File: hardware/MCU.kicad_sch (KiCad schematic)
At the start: 38 parts, among them J2 Micro_SD_Card, J3 USB_C_Receptacle, SW2 SW_Push, SW3 SW_Push, U7 ESP32-S3-WROOM-1, U8 WE-TVS-82400102

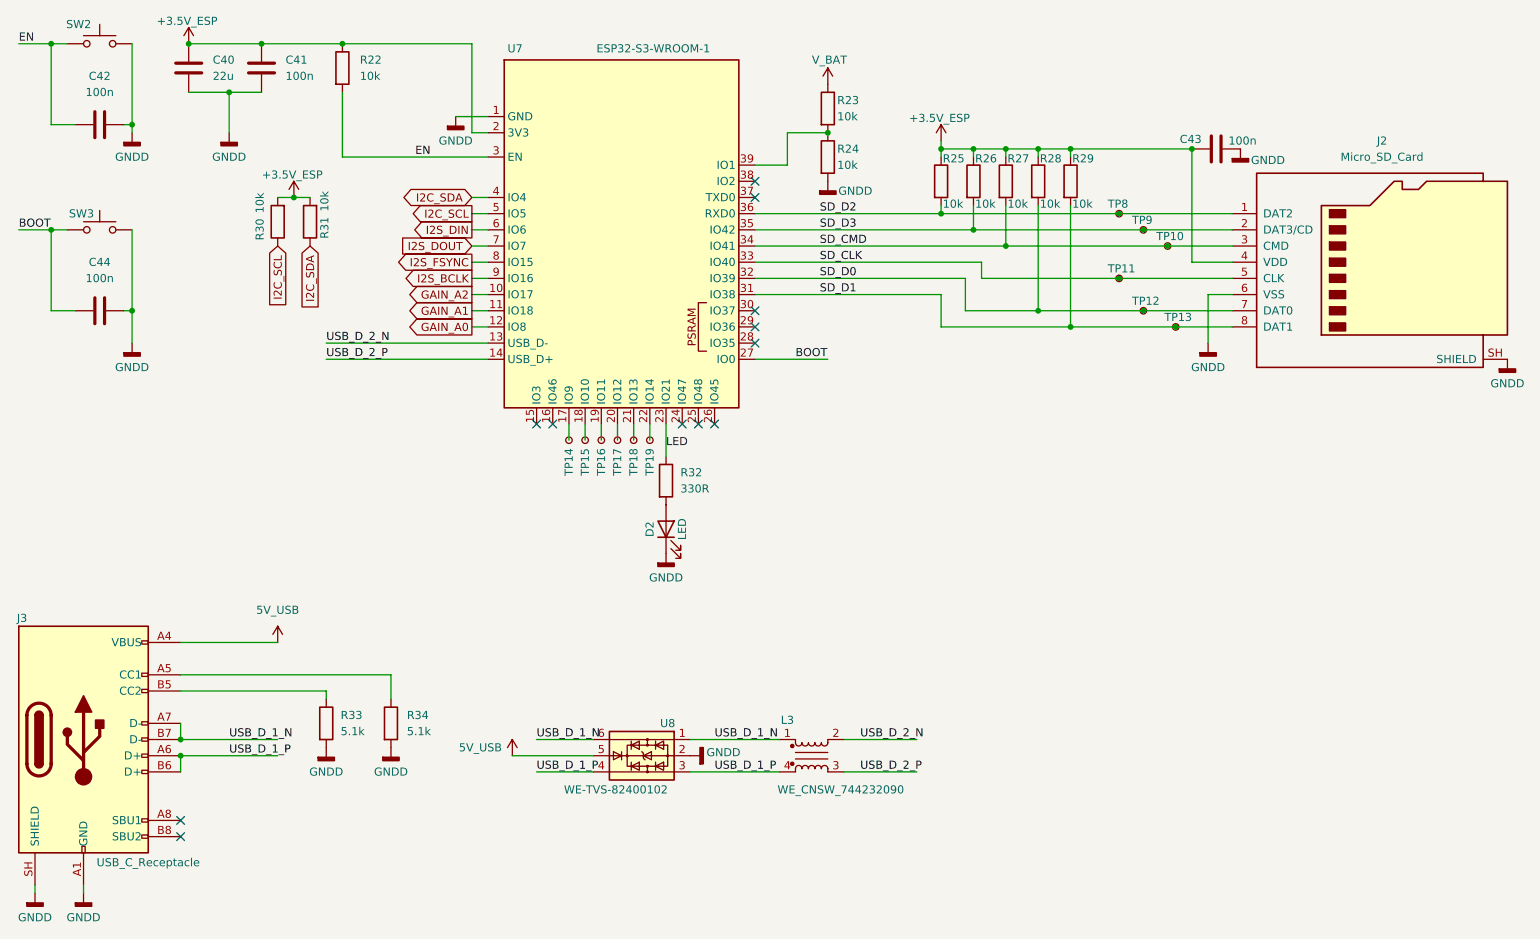
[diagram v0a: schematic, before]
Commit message: Changed Pinheader and found a Problem with V0CM.
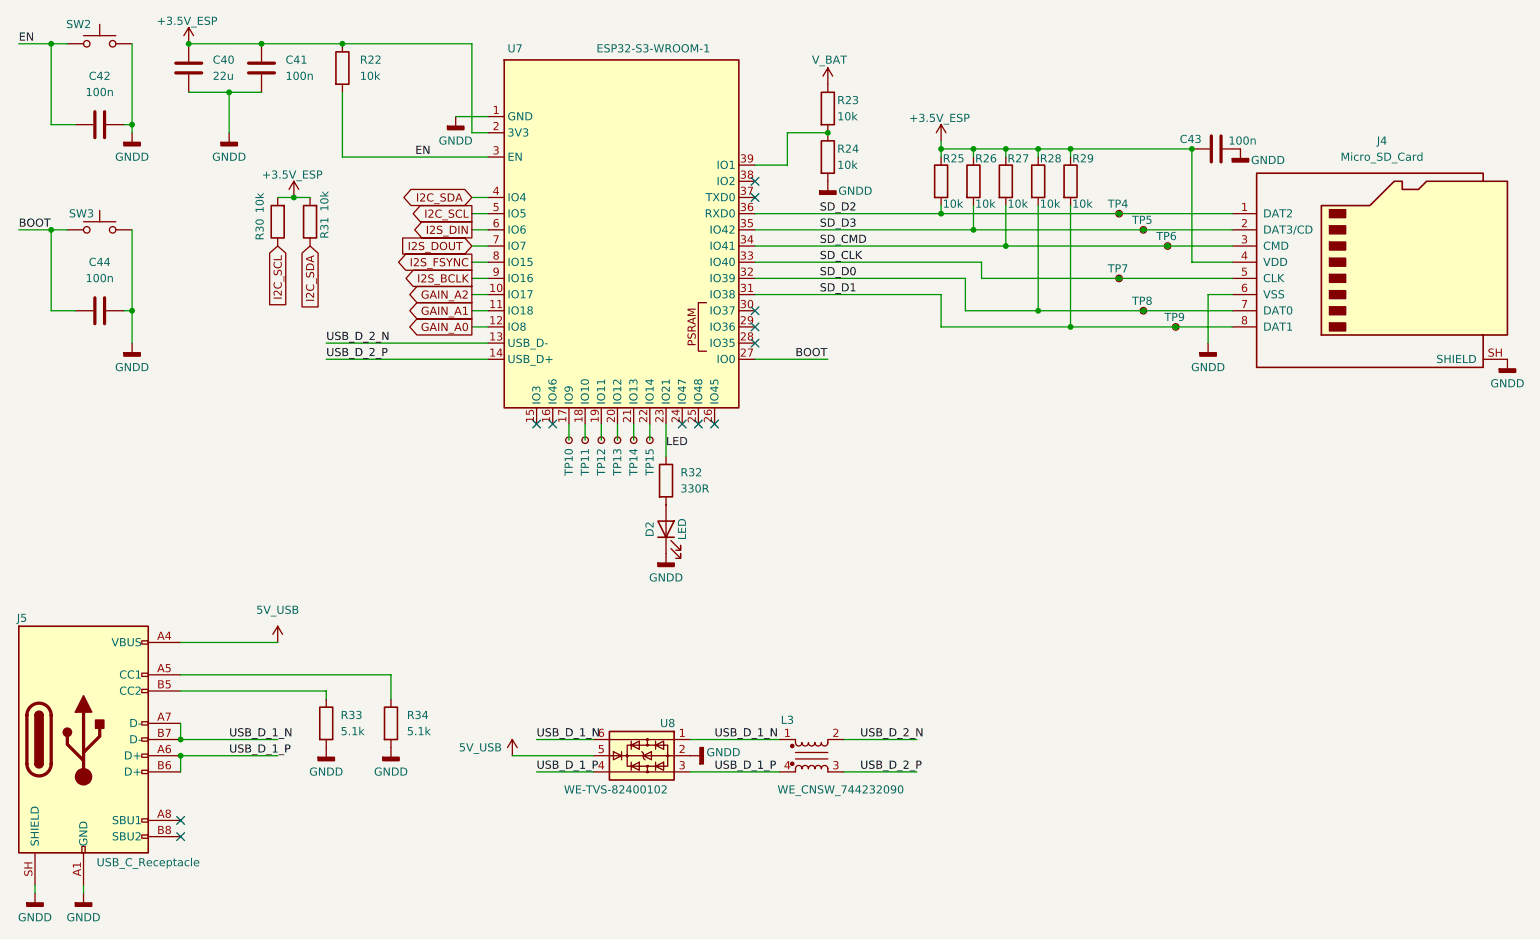
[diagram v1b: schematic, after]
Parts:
- renumbered J2 to J4, J3 to J5, TP14 to TP10, TP15 to TP11, TP16 to TP12, TP17 to TP13, TP18 to TP14, TP19 to TP15, TP8 to TP4, TP9 to TP5, TP10 to TP6, TP11 to TP7, TP12 to TP8, TP13 to TP9
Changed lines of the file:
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@@
 		(in_pos_files yes)
 		(dnp no)
-		(property "Reference" "TP16"
+		(property "Reference" "TP12"
 			(at 116.84 103.378 0)
 			(show_name no)
@@
 			(project "WirelessBERA"
 				(path "/9923f3cb-fea3-442a-b105-4e616c3606bf/59a77f1b-99cc-4fa7-8433-3094cca92854"
-					(reference "TP16")
+					(reference "TP12")
 					(unit 1)
 				)
@@
 		(in_pos_files yes)
 		(dnp no)
-		(property "Reference" "TP19"
+		(property "Reference" "TP15"
 			(at 124.46 103.378 0)
 			(show_name no)
@@
 			(project "WirelessBERA"
 				(path "/9923f3cb-fea3-442a-b105-4e616c3606bf/59a77f1b-99cc-4fa7-8433-3094cca92854"
-					(reference "TP19")
+					(reference "TP15")
 					(unit 1)
 				)
@@
 		(in_pos_files yes)
 		(dnp no)
-		(property "Reference" "J3"
+		(property "Reference" "J5"
 			(at 25.908 125.73 0)
 			(show_name no)
@@
 			(project "WirelessBERA"
 				(path "/9923f3cb-fea3-442a-b105-4e616c3606bf/59a77f1b-99cc-4fa7-8433-3094cca92854"
-					(reference "J3")
+					(reference "J5")
 					(unit 1)
 				)
@@
 		(in_pos_files yes)
 		(dnp no)
-		(property "Reference" "TP9"
+		(property "Reference" "TP5"
 			(at 200.152 63.246 0)
 			(show_name no)
@@
 			(project "WirelessBERA"
 				(path "/9923f3cb-fea3-442a-b105-4e616c3606bf/59a77f1b-99cc-4fa7-8433-3094cca92854"
-					(reference "TP9")
+					(reference "TP5")
 					(unit 1)
 				)
@@
 		(in_pos_files yes)
 		(dnp no)
-		(property "Reference" "TP10"
+		(property "Reference" "TP6"
 			(at 203.962 65.786 0)
 			(show_name no)
@@
 			(project "WirelessBERA"
 				(path "/9923f3cb-fea3-442a-b105-4e616c3606bf/59a77f1b-99cc-4fa7-8433-3094cca92854"
-					(reference "TP10")
+					(reference "TP6")
 					(unit 1)
 				)
@@
 		(dnp no)
 		(fields_autoplaced yes)
-		(property "Reference" "J2"
+		(property "Reference" "J4"
 			(at 239.395 50.8 0)
 			(show_name no)
@@
 			(project "WirelessBERA"
 				(path "/9923f3cb-fea3-442a-b105-4e616c3606bf/59a77f1b-99cc-4fa7-8433-3094cca92854"
-					(reference "J2")
+					(reference "J4")
 					(unit 1)
 				)
@@
 		(in_pos_files yes)
 		(dnp no)
-		(property "Reference" "TP17"
+		(property "Reference" "TP13"
 			(at 119.38 103.378 0)
 			(show_name no)
@@
 			(project "WirelessBERA"
 				(path "/9923f3cb-fea3-442a-b105-4e616c3606bf/59a77f1b-99cc-4fa7-8433-3094cca92854"
-					(reference "TP17")
+					(reference "TP13")
 					(unit 1)
 				)
@@
 		(in_pos_files yes)
 		(dnp no)
-		(property "Reference" "TP12"
+		(property "Reference" "TP8"
 			(at 200.152 75.946 0)
 			(show_name no)
@@
 			(project "WirelessBERA"
 				(path "/9923f3cb-fea3-442a-b105-4e616c3606bf/59a77f1b-99cc-4fa7-8433-3094cca92854"
-					(reference "TP12")
+					(reference "TP8")
 					(unit 1)
 				)
@@
 		(in_pos_files yes)
 		(dnp no)
-		(property "Reference" "TP18"
+		(property "Reference" "TP14"
 			(at 121.92 103.378 0)
 			(show_name no)
@@
 			(project "WirelessBERA"
 				(path "/9923f3cb-fea3-442a-b105-4e616c3606bf/59a77f1b-99cc-4fa7-8433-3094cca92854"
-					(reference "TP18")
+					(reference "TP14")
 					(unit 1)
 				)
@@
 		(in_pos_files yes)
 		(dnp no)
-		(property "Reference" "TP11"
+		(property "Reference" "TP7"
 			(at 196.342 70.866 0)
 			(show_name no)
@@
 			(project "WirelessBERA"
 				(path "/9923f3cb-fea3-442a-b105-4e616c3606bf/59a77f1b-99cc-4fa7-8433-3094cca92854"
-					(reference "TP11")
+					(reference "TP7")
 					(unit 1)
 				)
@@
 		(in_pos_files yes)
 		(dnp no)
-		(property "Reference" "TP13"
+		(property "Reference" "TP9"
 			(at 205.232 78.486 0)
 			(show_name no)
@@
 			(project "WirelessBERA"
 				(path "/9923f3cb-fea3-442a-b105-4e616c3606bf/59a77f1b-99cc-4fa7-8433-3094cca92854"
-					(reference "TP13")
+					(reference "TP9")
 					(unit 1)
 				)
@@
 		(in_pos_files yes)
 		(dnp no)
-		(property "Reference" "TP8"
+		(property "Reference" "TP4"
 			(at 196.342 60.706 0)
 			(show_name no)
@@
 			(project "WirelessBERA"
 				(path "/9923f3cb-fea3-442a-b105-4e616c3606bf/59a77f1b-99cc-4fa7-8433-3094cca92854"
-					(reference "TP8")
+					(reference "TP4")
 					(unit 1)
 				)
@@
 		(in_pos_files yes)
 		(dnp no)
-		(property "Reference" "TP15"
+		(property "Reference" "TP11"
 			(at 114.3 103.378 0)
 			(show_name no)
@@
 			(project "WirelessBERA"
 				(path "/9923f3cb-fea3-442a-b105-4e616c3606bf/59a77f1b-99cc-4fa7-8433-3094cca92854"
-					(reference "TP15")
+					(reference "TP11")
 					(unit 1)
 				)
@@
 		(in_pos_files yes)
 		(dnp no)
-		(property "Reference" "TP14"
+		(property "Reference" "TP10"
 			(at 111.76 103.378 0)
 			(show_name no)
@@
 			(project "WirelessBERA"
 				(path "/9923f3cb-fea3-442a-b105-4e616c3606bf/59a77f1b-99cc-4fa7-8433-3094cca92854"
-					(reference "TP14")
+					(reference "TP10")
 					(unit 1)
 				)
